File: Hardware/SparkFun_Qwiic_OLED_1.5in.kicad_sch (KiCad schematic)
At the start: 39 parts, among them J1 Qwiic_RA, J2 Qwiic_RA, J3 Conn_01x06, J4 Conn_01x24_FPC, U2 WEO128128ASAP3N00000, U5 AP3012

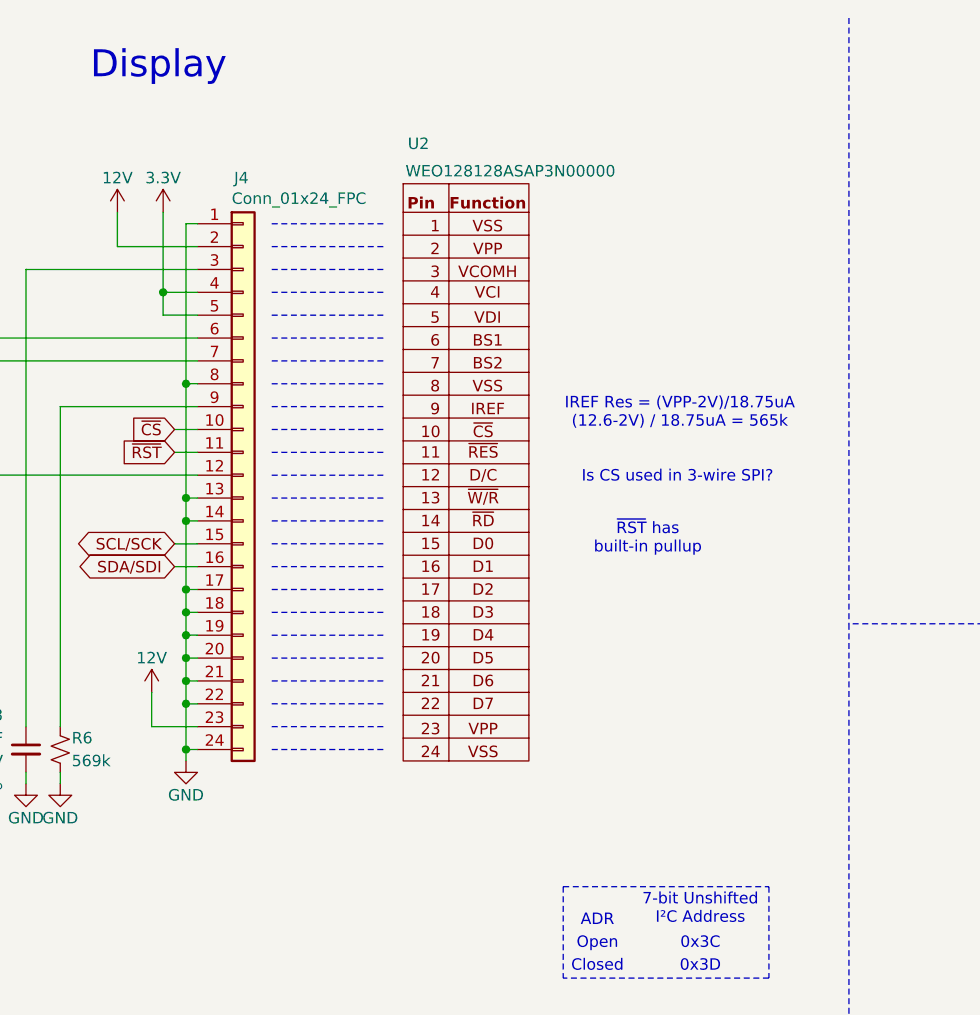
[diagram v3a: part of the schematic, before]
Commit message: Aligns the power circuitry to the IC's specification
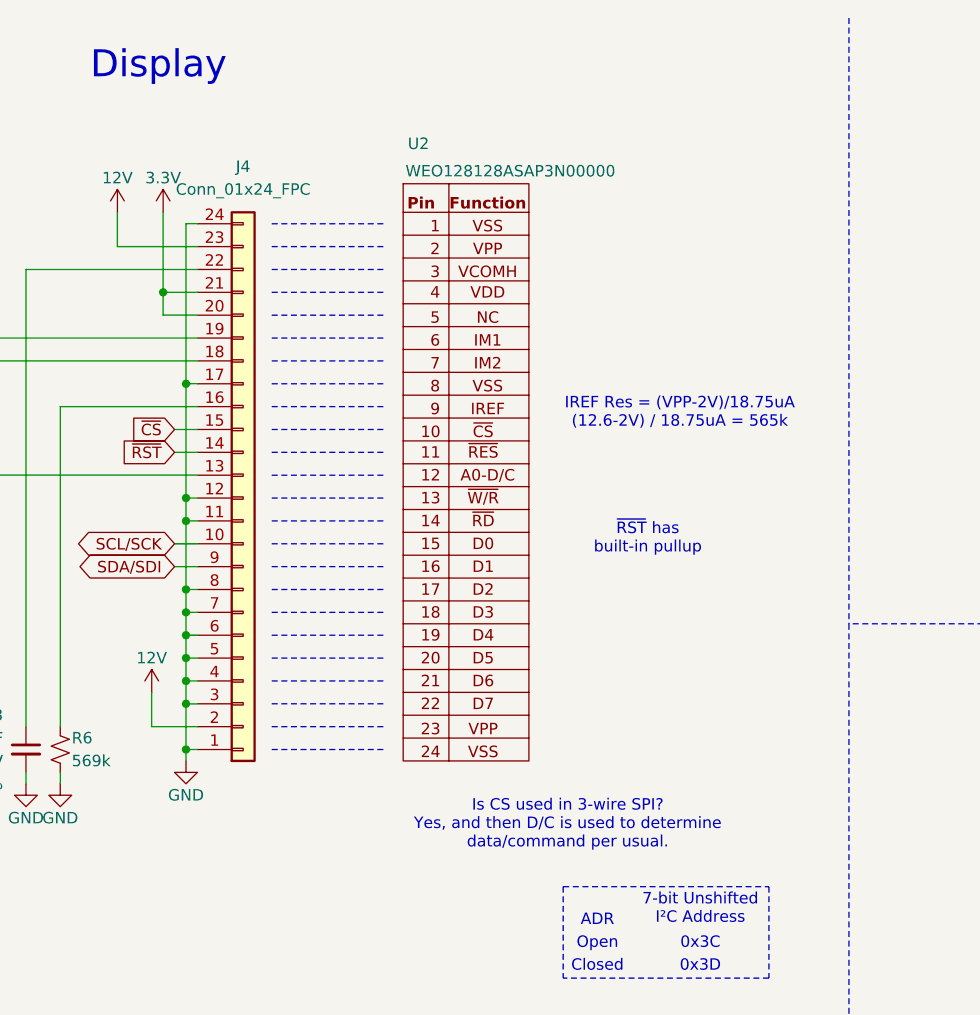
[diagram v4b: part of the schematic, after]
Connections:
- net 3.3V: now also J4.20 (Pin_20), J4.21 (Pin_21); no longer J4.4 (Pin_4), J4.5 (Pin_5)
- net GND: now also J4.11 (Pin_11), J4.12 (Pin_12), J4.3 (Pin_3), J4.4 (Pin_4), J4.5 (Pin_5), J4.6 (Pin_6), J4.7 (Pin_7); no longer J4.13 (Pin_13), J4.14 (Pin_14), J4.18 (Pin_18), J4.19 (Pin_19), J4.20 (Pin_20), J4.21 (Pin_21), J4.22 (Pin_22)
- net SCL/SCK: now also J4.10 (Pin_10); no longer J4.15 (Pin_15)
- net SDA/SDI: now also J4.9 (Pin_9); no longer J4.16 (Pin_16)
- net ~{CS}: now also J4.15 (Pin_15); no longer J4.10 (Pin_10)
- net ~{RST}: now also J4.14 (Pin_14); no longer J4.11 (Pin_11)
- net at JP6.2 (B), R10.2: now also J4.19 (Pin_19); no longer J4.6 (Pin_6)
- net at R6.2: now also J4.16 (Pin_16); no longer J4.9 (Pin_9)
- net at C3.1: now also J4.22 (Pin_22); no longer J4.3 (Pin_3)
- net at JP3.1 (A), R7.2: now also J4.13 (Pin_13); no longer J4.12 (Pin_12)
- net at JP7.1 (A), R11.1: now also J4.18 (Pin_18); no longer J4.7 (Pin_7)
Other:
- note added: "Is CS used in 3-wire SPI? Yes, and then D/C is used to determine data/command per usual."
- note removed: "Is CS used in 3-wire SPI?"
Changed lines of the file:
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@@
 		)
 	)
-	(text "Is CS used in 3-wire SPI?"
+	(text "Is CS used in 3-wire SPI?\nYes, and then D/C is used to determine\ndata/command per usual. "
 		(exclude_from_sim no)
-		(at 140.97 65.024 0)
+		(at 128.778 103.632 0)
 		(effects
 			(font
@@
 	)
 	(symbol
-		(lib_id "SparkFun-Connector:Conn_01x24_FPC_0.5mm")
-		(at 92.71 62.23 0)
-		(unit 1)
-		(exclude_from_sim no)
-		(in_bom yes)
-		(on_board yes)
-		(dnp no)
-		(property "Reference" "J4"
-			(at 91.694 31.75 0)
-			(effects
-				(font
-					(size 1.27 1.27)
-				)
-				(justify left)
-			)
-		)
-		(property "Value" "Conn_01x24_FPC"
-			(at 91.44 34.036 0)
-			(effects
-				(font
-					(size 1.27 1.27)
-				)
-				(justify left)
-			)
-		)
-		(property "Footprint" "SparkFun-Connector:FPC_0.5mm-24"
-			(at 93.218 100.33 0)
-			(effects
-				(font
-					(size 1.27 1.27)
-				)
-				(hide yes)
-			)
-		)
-		(property "Datasheet" "https://www.atom-connector.com/uploads/FPC0.5mm-XP-SMTH1.5.pdf"
-			(at 93.218 102.87 0)
-			(effects
-				(font
-					(size 1.27 1.27)
-				)
-				(hide yes)
-			)
-		)
-		(property "Description" "FPC connector 24-pin 0.5mm"
-			(at 92.71 105.41 0)
-			(effects
-				(font
-					(size 1.27 1.27)
-				)
-				(hide yes)
-			)
-		)
-		(property "PROD_ID" "CONN-14195"
-			(at 92.71 107.95 0)
-			(effects
-				(font
-					(size 1.27 1.27)
-				)
-				(hide yes)
-			)
-		)
-		(pin "10"
-		)
-		(pin "14"
-		)
-		(pin "15"
-		)
-		(pin "18"
-		)
-		(pin "5"
-		)
-		(pin "13"
-		)
-		(pin "9"
-		)
-		(pin "8"
-		)
-		(pin "23"
-		)
-		(pin "6"
-		)
-		(pin "20"
-		)
-		(pin "2"
-		)
-		(pin "17"
-		)
-		(pin "24"
-		)
-		(pin "MP1"
-		)
-		(pin "7"
-		)
-		(pin "11"
-		)
-		(pin "12"
-		)
-		(pin "21"
-		)
-		(pin "22"
-		)
-		(pin "4"
-		)
-		(pin "3"
-		)
-		(pin "19"
-		)
-		(pin "1"
-		)
-		(pin "16"
-		)
-		(pin "MP2"
-		)
-		(instances
-			(project "SparkFun_Qwiic_OLED_1.5in"
-				(path "/e3dd3ae4-244d-4cba-9cca-5d2abf83f29a"
-					(reference "J4")
-					(unit 1)
-				)
-			)
-		)
-	)
-	(symbol
 		(lib_id "SparkFun-IC-Power:AP3012")
 		(at 205.74 49.53 0)
@@
 					(unit 1)
 				)
+			)
+		)
+	)
+	(symbol
+		(lib_id "SparkFun-Connector:Conn_01x24_FPC_0.5mm")
+		(at 92.71 69.85 0)
+		(mirror x)
+		(unit 1)
+		(exclude_from_sim no)
+		(in_bom yes)
+		(on_board yes)
+		(dnp no)
+		(fields_autoplaced yes)
+		(property "Reference" "J4"
+			(at 92.71 30.48 0)
+			(effects
+				(font
+					(size 1.27 1.27)
+				)
+			)
+		)
+		(property "Value" "Conn_01x24_FPC"
+			(at 92.71 33.02 0)
+			(effects
+				(font
+					(size 1.27 1.27)
+				)
+			)
+		)
+		(property "Footprint" "SparkFun-Connector:FPC_0.5mm-24"
+			(at 93.218 31.75 0)
+			(effects
+				(font
+					(size 1.27 1.27)
+				)
+				(hide yes)
+			)
+		)
+		(property "Datasheet" "https://www.atom-connector.com/uploads/FPC0.5mm-XP-SMTH1.5.pdf"
+			(at 93.218 29.21 0)
+			(effects
+				(font
+					(size 1.27 1.27)
+				)
+				(hide yes)
+			)
+		)
+		(property "Description" "FPC connector 24-pin 0.5mm"
+			(at 92.71 26.67 0)
+			(effects
+				(font
+					(size 1.27 1.27)
+				)
+				(hide yes)
+			)
+		)
+		(property "PROD_ID" "CONN-14195"
+			(at 92.71 24.13 0)
+			(effects
+				(font
+					(size 1.27 1.27)
+				)
+				(hide yes)
+			)
+		)
+		(pin "10"
+		)
+		(pin "12"
+		)
+		(pin "3"
+		)
+		(pin "4"
+		)
+		(pin "5"
+		)
+		(pin "1"
+		)
+		(pin "2"
+		)
+		(pin "6"
+		)
+		(pin "7"
+		)
+		(pin "8"
+		)
+		(pin "9"
+		)
+		(pin "11"
+		)
+		(pin "13"
+		)
+		(pin "14"
+		)
+		(pin "15"
+		)
+		(pin "16"
+		)
+		(pin "17"
+		)
+		(pin "22"
+		)
+		(pin "18"
+		)
+		(pin "24"
+		)
+		(pin "21"
+		)
+		(pin "23"
+		)
+		(pin "MP2"
+		)
+		(pin "20"
+		)
+		(pin "MP1"
+		)
+		(pin "19"
+		)
+		(instances
+			(project ""
+				(path "/e3dd3ae4-244d-4cba-9cca-5d2abf83f29a"
+					(reference "J4")
+					(unit 1)
+				)

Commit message: Routes the power circuitry
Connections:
- net 12V_OUT: now reaches D2.2 (A), L1.2, U5.1 (SW)
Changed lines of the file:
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@@
+	)
+	(junction
+		(at 214.63 38.1)
+		(diameter 0)
+		(color 0 0 0 0)
 	)
 	(junction
@@
 	(wire
 		(pts
-			(xy 208.28 38.1) (xy 217.17 38.1)
+			(xy 208.28 38.1) (xy 214.63 38.1)
 		)
 		(stroke
@@
 	(wire
 		(pts
+			(xy 226.06 30.48) (xy 214.63 30.48)
+		)
+		(stroke
+			(width 0)
+			(type default)
+		)
+	)
+	(wire
+		(pts
 			(xy 40.64 59.69) (xy 40.64 55.88)
 		)
@@
 	(wire
 		(pts
+			(xy 214.63 38.1) (xy 217.17 38.1)
+		)
+		(stroke
+			(width 0)
+			(type default)
+		)
+	)
+	(wire
+		(pts
 			(xy 86.36 82.55) (xy 86.36 85.09)
 		)
@@
 	(wire
 		(pts
+			(xy 214.63 30.48) (xy 214.63 38.1)
+		)
+		(stroke
+			(width 0)
+			(type default)
+		)
+	)
+	(wire
+		(pts
 			(xy 205.74 58.42) (xy 205.74 57.15)
 		)
@@
 		)
 	)
+	(global_label "12V_OUT"
+		(shape output)
+		(at 226.06 30.48 0)
+		(fields_autoplaced yes)
+		(effects
+			(font
+				(size 1.27 1.27)
+			)
+			(justify left)
+		)
+		(property "Intersheetrefs" "${INTERSHEET_REFS}"
+			(at 237.149 30.48 0)
+			(effects
+				(font
+					(size 1.27 1.27)
+				)
+				(justify left)
+				(hide yes)
+			)
+		)
+	)

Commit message: Changes the 12V_OUT label to be more discrete
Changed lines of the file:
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@@
-	)
-	(junction
-		(at 214.63 38.1)
-		(diameter 0)
-		(color 0 0 0 0)
 	)
 	(junction
@@
 	(wire
 		(pts
-			(xy 208.28 38.1) (xy 214.63 38.1)
+			(xy 208.28 38.1) (xy 217.17 38.1)
 		)
 		(stroke
@@
 	(wire
 		(pts
-			(xy 226.06 30.48) (xy 214.63 30.48)
-		)
-		(stroke
-			(width 0)
-			(type default)
-		)
-	)
-	(wire
-		(pts
 			(xy 40.64 59.69) (xy 40.64 55.88)
 		)
@@
 	(wire
 		(pts
-			(xy 214.63 38.1) (xy 217.17 38.1)
-		)
-		(stroke
-			(width 0)
-			(type default)
-		)
-	)
-	(wire
-		(pts
 			(xy 86.36 82.55) (xy 86.36 85.09)
 		)
@@
 	(wire
 		(pts
-			(xy 214.63 30.48) (xy 214.63 38.1)
-		)
-		(stroke
-			(width 0)
-			(type default)
-		)
-	)
-	(wire
-		(pts
 			(xy 205.74 58.42) (xy 205.74 57.15)
 		)
@@
 		)
 	)
-	(global_label "12V_OUT"
-		(shape output)
-		(at 226.06 30.48 0)
-		(fields_autoplaced yes)
+	(label "12V_OUT"
+		(at 209.55 38.1 0)
 		(effects
 			(font
 				(size 1.27 1.27)
 			)
-			(justify left)
-		)
-		(property "Intersheetrefs" "${INTERSHEET_REFS}"
-			(at 237.149 30.48 0)
-			(effects
-				(font
-					(size 1.27 1.27)
-				)
-				(justify left)
-				(hide yes)
-			)
-		)
-	)
+			(justify left bottom)
+		)
+	)

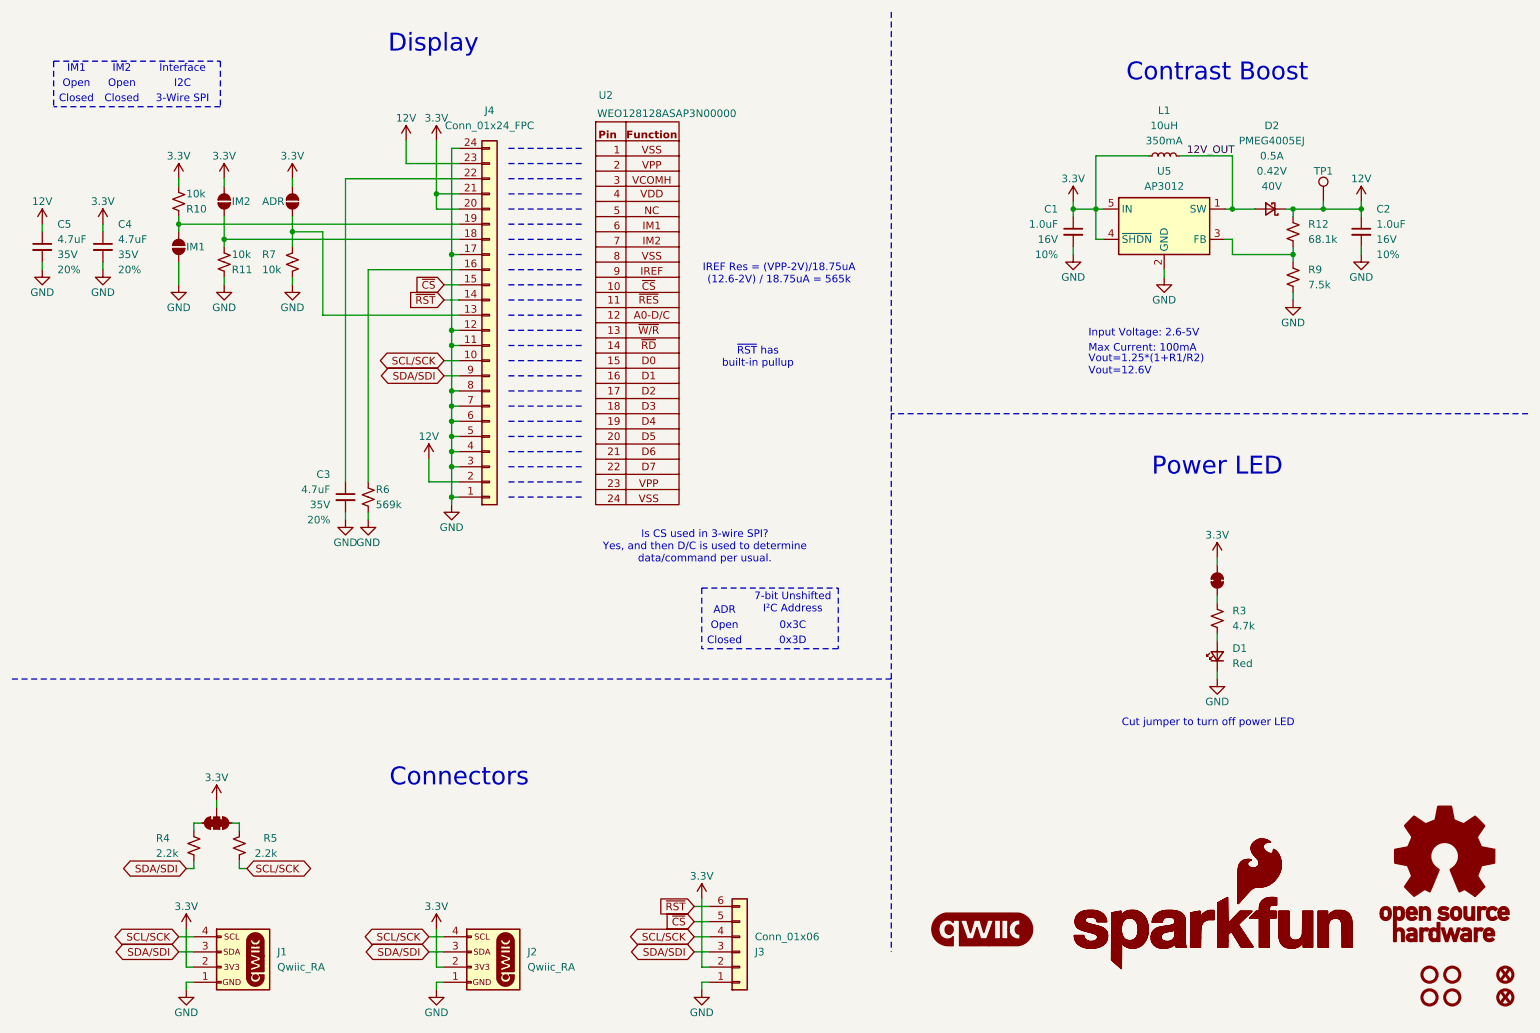
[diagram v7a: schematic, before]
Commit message: Updates the text within the schematic to be more clear
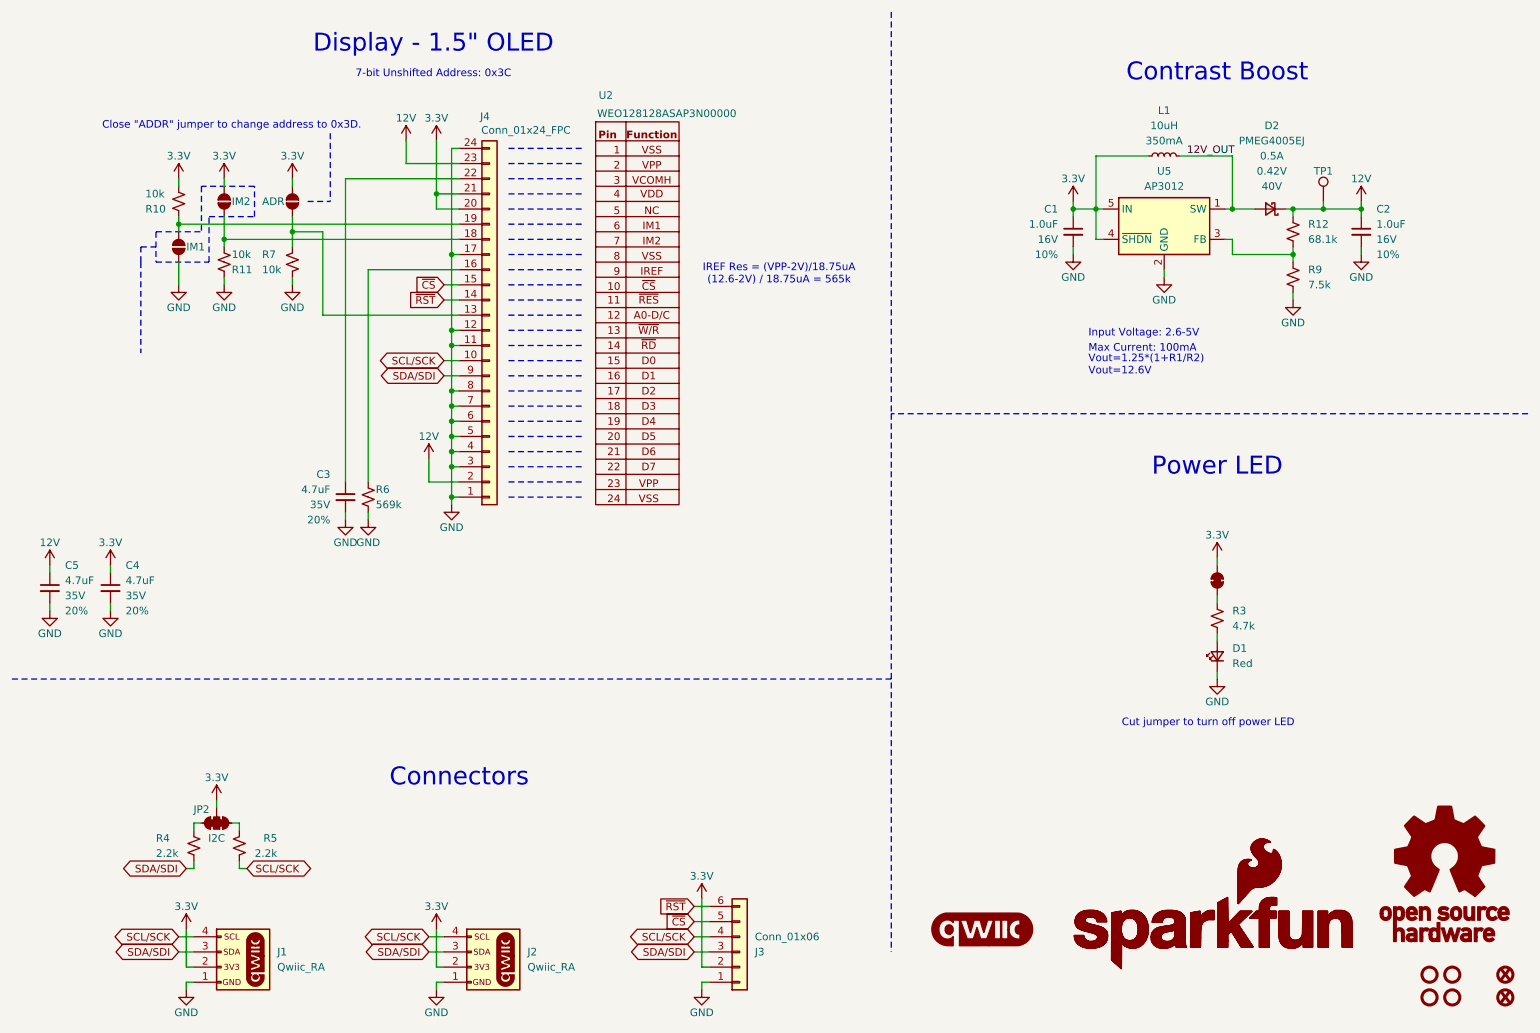
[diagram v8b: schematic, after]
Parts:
- JP2: value ~ -> I2C
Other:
- note added: "7-bit Unshifted Address: 0x3C"
- note added: "Close "ADDR" jumper to change address to 0x3D."
- note added: "Display - 1.5" OLED"
- note removed: "0x3C"
- note removed: "0x3D"
- note removed: "3-Wire SPI"
- note removed: "7-bit Unshifted I²C Address"
- note removed: "ADR"
- note removed: "Closed"
- note removed: "Display"
- note removed: "I2C"
- note removed: "IM1"
- note removed: "IM2"
- note removed: "Interface"
- note removed: "Is CS used in 3-wire SPI? Yes, and then D/C is used to determine data/command per usual."
- note removed: "Open"
- note removed: "~{RST} has built-in pullup"
- moved on the sheet: C4, C5
